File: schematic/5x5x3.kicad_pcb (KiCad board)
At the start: 4 copper layers, 204 x 100 mm, 208 parts, among them J1 SW Debug, J10 Conn_01x03_Female, J11 Conn_01x03_Male, J12 Conn_01x03_Male, J13 Conn_01x03_Female, J14 Conn_01x03_Female, J15 Conn_01x03_Male, J16 Conn_01x03_Female, J2 Battery, J3 Conn_01x03_Male, J4 Conn_01x03_Male, J5 Conn_01x03_Female, J6 Conn_01x03_Female, J7 Conn_01x03_Male, J8 Conn_01x03_Male, J9 Conn_01x03_Female, SW11 SW, SW12 SW, SW13 SW, SW14 SW, SW21 SW, SW22 SW, SW23 SW, SW24 SW, SW25 SW, SW31 SW, SW32 SW, SW33 SW, SW34 SW, SW35 SW, SW41 SW, SW42 SW, SW43 SW, SW44 SW, SW45 SW, SW51 SW, SW52 SW, SW53 SW, SW54 SW, SW55 SW, SW6 ALPS_EC11, U1 nice_nano v2

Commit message: Keyboard routed, added kibuzzard labels on mcu board
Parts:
- removed the J1 at (249.9, 104.2)
- removed the kibuzzard-62AF73B1 at (206.5, 43.6)
- removed the kibuzzard-62AF73B1 at (171.0, 43.6)
- removed the kibuzzard-62AF73B1 at (168.5, 43.6)
- removed the kibuzzard-62AF73D1 at (209.0, 43.2)
- removed the kibuzzard-62AF73D1 at (173.6, 43.2)
- removed the kibuzzard-62AF73D1 at (211.6, 43.2)
- removed kibuzzard-62AF7423: G***, kibuzzard-62AF7423
- removed kibuzzard-62AF742E: G***, kibuzzard-62AF742E
- removed the kibuzzard-62AF7487 at (206.5, 133.1)
- removed the kibuzzard-62AF7492 at (209.0, 133.1)
- removed the kibuzzard-62AF749F at (211.6, 133.1)
- removed the kibuzzard-62AF74B5 at (168.5, 133.1)
- removed the kibuzzard-62AF74BF at (171.0, 133.1)
- removed the kibuzzard-62AF74C8 at (173.6, 133.1)
- removed kibuzzard-62AF74DA: G***, kibuzzard-62AF74DA
- removed kibuzzard-62AF74E3: G***, kibuzzard-62AF74E3
- removed kibuzzard-62AF74EC: G***, kibuzzard-62AF74EC
- removed kibuzzard-62AF74F7: G***, kibuzzard-62AF74F7
- removed kibuzzard-62AF74FE: G***, kibuzzard-62AF74FE
- removed kibuzzard-62AF750A: G***, kibuzzard-62AF750A
- removed the kibuzzard-62AF7A14 at (235.0, 103.2)
- removed the kibuzzard-62AF7A28 at (234.2, 105.8)
- removed the kibuzzard-62AF7A49 at (234.2, 108.2)
- removed the kibuzzard-62AF7A56 at (235.0, 110.8)
- added kibuzzard-68B42C08: G***, kibuzzard-68B42C08, F.Cu at (173.6, 44.2)
- added kibuzzard-68B4713C: G***, kibuzzard-68B4713C, F.Cu at (206.5, 43.8)
- added kibuzzard-68B4713C: G***, kibuzzard-68B4713C, F.Cu at (171.0, 43.8)
- added kibuzzard-68B4713C: G***, kibuzzard-68B4713C, F.Cu at (168.5, 43.8)
- added kibuzzard-68B4715A: G***, kibuzzard-68B4715A, F.Cu at (211.6, 44.2)
- added kibuzzard-68B47169: G***, kibuzzard-68B47169, F.Cu at (209.0, 44.2)
- added kibuzzard-68B471AC: G***, kibuzzard-68B471AC, F.Cu at (145.3, 66.5)
- added kibuzzard-68B471BD: G***, kibuzzard-68B471BD, F.Cu at (145.3, 69.1)
- added kibuzzard-68B471DE: G***, kibuzzard-68B471DE, F.Cu at (145.3, 71.7)
- added kibuzzard-68B471FE: G***, kibuzzard-68B471FE, F.Cu at (145.2, 104.4)
- added kibuzzard-68B47213: G***, kibuzzard-68B47213, F.Cu at (145.2, 106.9)
- added kibuzzard-68B4721A: G***, kibuzzard-68B4721A, F.Cu at (145.2, 109.5)
- added kibuzzard-68B47243: G***, kibuzzard-68B47243, F.Cu at (234.8, 69.0)
- added kibuzzard-68B4724C: G***, kibuzzard-68B4724C, F.Cu at (234.8, 71.6)
- added kibuzzard-68B4727C: G***, kibuzzard-68B4727C, F.Cu at (234.1, 103.3)
- added kibuzzard-68B4728F: G***, kibuzzard-68B4728F, F.Cu at (233.3, 105.7)
- added kibuzzard-68B472A1: G***, kibuzzard-68B472A1, F.Cu at (233.3, 108.2)
- added kibuzzard-68B472AB: G***, kibuzzard-68B472AB, F.Cu at (234.2, 110.7)
- added kibuzzard-68B47320: G***, kibuzzard-68B47320, F.Cu at (168.5, 132.8)
- added kibuzzard-68B47329: G***, kibuzzard-68B47329, F.Cu at (171.1, 132.8)
- added kibuzzard-68B47332: G***, kibuzzard-68B47332, F.Cu at (173.6, 132.8)
- added kibuzzard-68B4733A: G***, kibuzzard-68B4733A, F.Cu at (206.5, 132.8)
- added kibuzzard-68B47346: G***, kibuzzard-68B47346, F.Cu at (209.0, 132.8)
- added kibuzzard-68B47351: G***, kibuzzard-68B47351, F.Cu at (211.6, 132.8)
- J2, PWSW1: moved to F.Cu
- moved PWSW1 55.1 mm to (221.9, 39.8), turned to 0 degrees
- moved J2 33.3 mm to (221.9, 47.8), turned to 180 degrees
- moved R15 19.6 mm to (133.8, 55.6), turned to 90 degrees
- moved R18 19.5 mm to (131.2, 55.6), turned to 90 degrees
- moved U1 1.91 mm to (190.3, 55.8)
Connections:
- J1 pad 1: +3V3 -> Vbatt
- J1 pad 2: Net-(C_R1-Pad2) -> SWDIO
- J1 pad 3: Net-(C_R2-Pad1) -> SWCLK
- J3 pad 3: Vext -> Vpowered
- J4 pad 2: Vusb -> Vext
- J4 pad 3: Vusb -> Vext
- J5 pad 3: Vusb -> Vpowered
- J6 pad 2: Vusb -> Vext
- J6 pad 3: Vusb -> Vext
- LED55 pad 2: Net-(LED55-DOUT) -> BACKLIGHTOUT
- R20 pad 1: Net-(LED55-DOUT) -> BACKLIGHTOUT
- U1 pad 5: BACKLIGHTIN -> unconnected-(U1-P0.17-Pad5)
- U1 pad 7: unconnected-(U1-P0.22-Pad7) -> BACKLIGHTIN
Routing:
- net Vpowered: track 1.64 -> 69.7 mm, vias 0 -> 1
- net ROTB: track 0.08 -> 16.1 mm
- net ROTA: track 0.11 -> 13.7 mm
- net Net-(C19-Pad1): track 6.49 -> 13.1 mm
- net COL5: track 111.5 -> 105.6 mm
- net Net-(LED55-DOUT): track 5.40 -> 0.00 mm
- net BACKLIGHTOUT: track 30.3 -> 35.7 mm
- net Net-(C20-Pad1): track 5.24 -> 7.42 mm

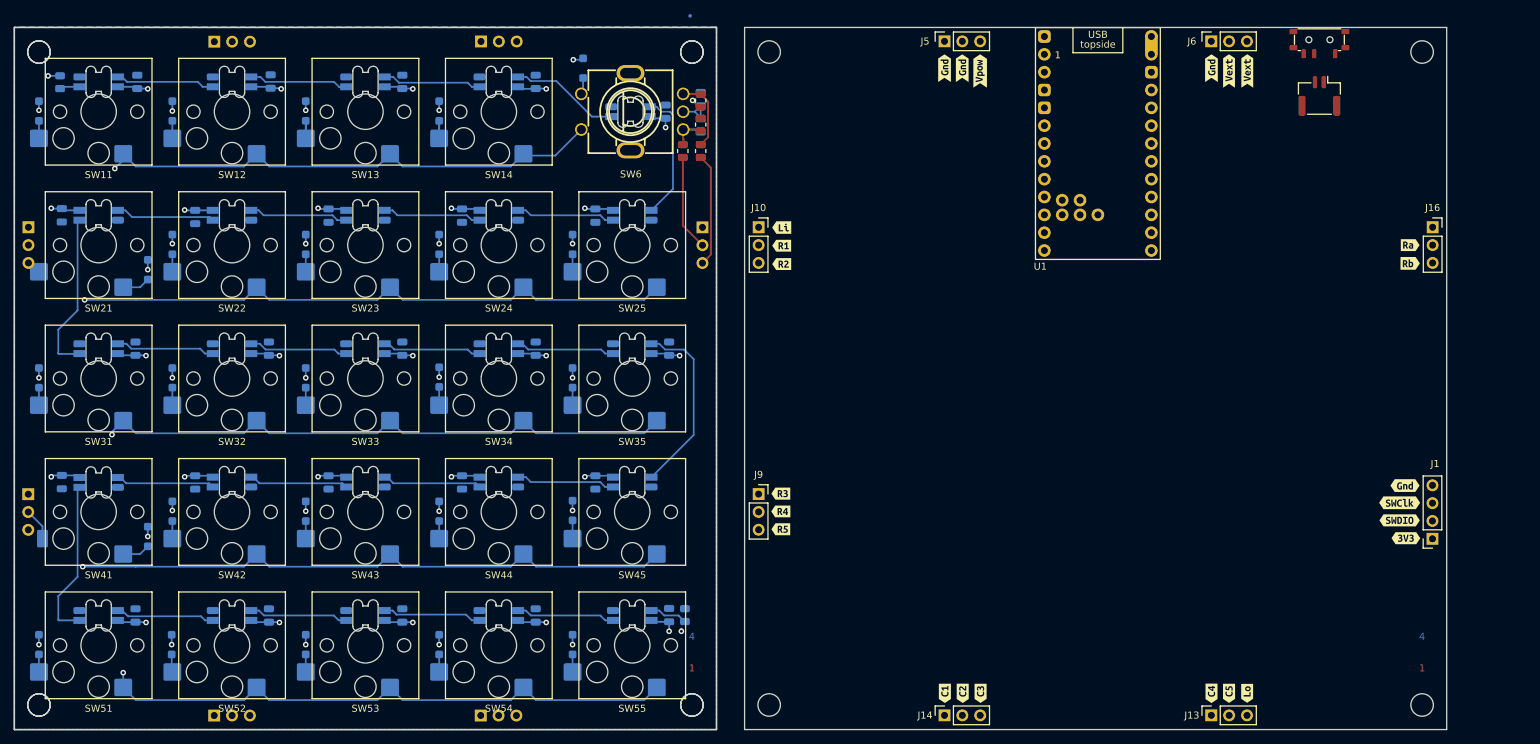
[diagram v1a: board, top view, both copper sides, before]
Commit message: Adjusted layer indications, component label legibility, routed mcu
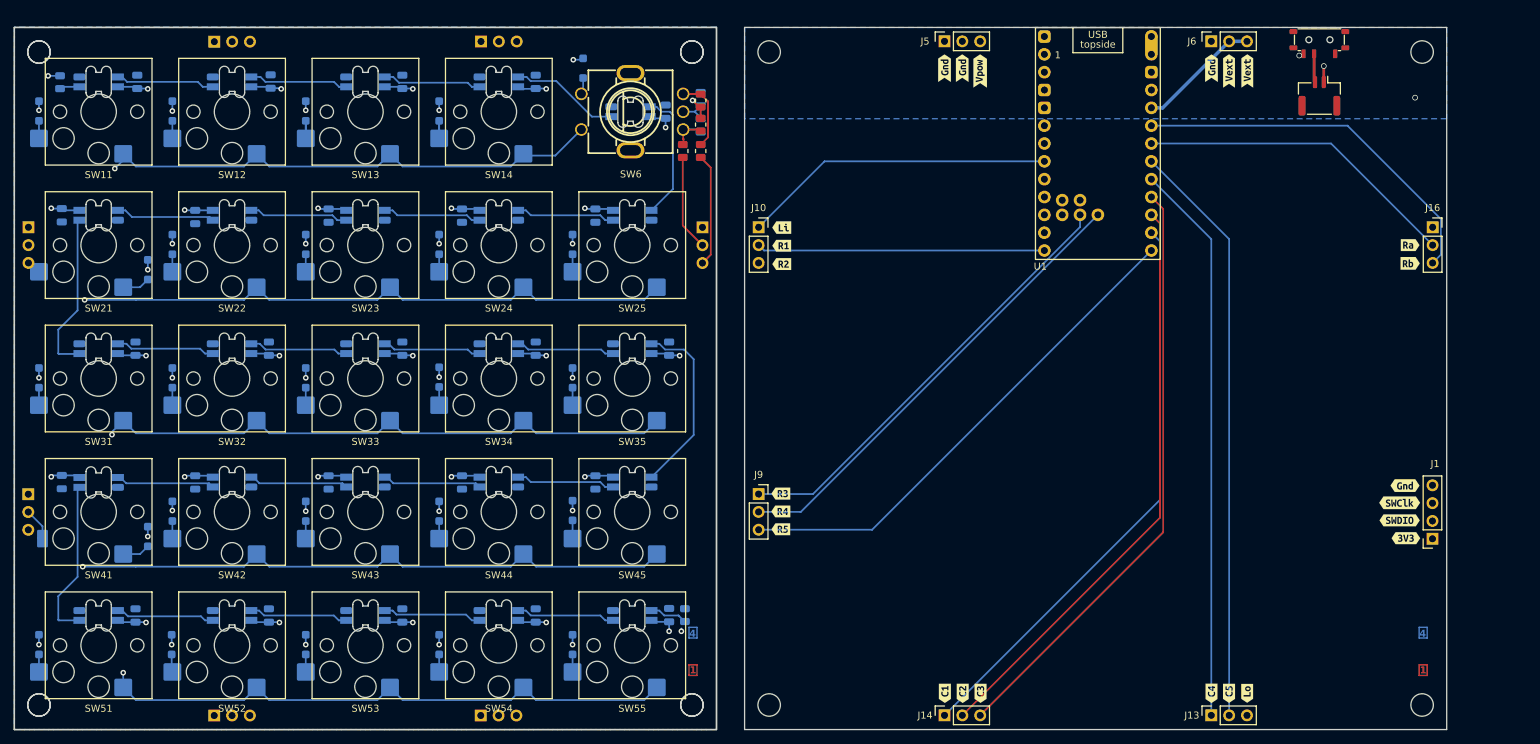
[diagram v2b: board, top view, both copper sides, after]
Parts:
- removed the G*** at (131.2, 112.8)
- removed kibuzzard-62AF73B1 (x3): G***, kibuzzard-62AF73B1
- removed kibuzzard-62AF73D1 (x3): G***, kibuzzard-62AF73D1
- added kibuzzard-68B42C08: G***, kibuzzard-68B42C08, B.Cu at (173.5, 44.2)
- added kibuzzard-68B4713C: G***, kibuzzard-68B4713C, B.Cu at (206.5, 43.8)
- added kibuzzard-68B4713C: G***, kibuzzard-68B4713C, B.Cu at (171.0, 43.8)
- added kibuzzard-68B4713C: G***, kibuzzard-68B4713C, B.Cu at (168.5, 43.8)
- added kibuzzard-68B4715A: G***, kibuzzard-68B4715A, B.Cu at (211.6, 44.2)
- added kibuzzard-68B47169: G***, kibuzzard-68B47169, B.Cu at (209.0, 44.2)
- moved kibuzzard-685E981C 80.5 mm to (225.1, 40.0), turned to 180 degrees
- moved kibuzzard-685E9829 72.7 mm to (219.6, 40.0), turned to 180 degrees
- moved G*** 20.4 mm to (97.0, 116.6)
- moved kibuzzard-62AF6BA3 3.96 mm to (38.0, 74.5), turned to 90 degrees
- moved kibuzzard-62AF6B7C 3.94 mm to (38.0, 112.5), turned to 90 degrees
- moved kibuzzard-62AF6BAD 0.61 mm to (40.8, 68.5)
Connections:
- J1 pad 1: Vbatt -> Vpowered
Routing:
- net Vpowered: track 69.7 -> 208.2 mm, vias 1 -> 2
- net COL3: track 96.3 -> 181.6 mm
- net COL5: track 105.6 -> 189.1 mm
- net COL2: track 97.4 -> 180.8 mm
- net COL1: track 147.7 -> 229.7 mm
- net COL4: track 95.5 -> 175.4 mm
- net ROW5: track 112.6 -> 185.0 mm
- net SWDIO: track 0.00 -> 72.2 mm
- net SWCLK: track 0.00 -> 68.5 mm
- net ROW4: track 104.1 -> 170.0 mm
- net ROW3: track 102.1 -> 165.4 mm
- net GND: track 6.05 -> 64.6 mm, vias 0 -> 2
- net ROTB: track 16.1 -> 69.6 mm
- net ROW2: track 96.9 -> 143.0 mm
- net ROTA: track 13.7 -> 59.7 mm
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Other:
- board text added: "202509"
- board text removed: "202206"
